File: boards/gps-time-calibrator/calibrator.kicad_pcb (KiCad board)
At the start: 4 copper layers, 180 x 100 mm, 368 parts, among them J1 DF40C-40DP-0.4V(51), J2 DF40C(2.0)-40DS-0.4V(51), J3 USB-C 5V/3A + DATA, J5 GPS ANTENNA, J6 INPUT 5V / 2.5V THRESHOLD, J7 FPGA OUTPUT 5V, J8 61300411121, Q1 AO3400A, Q10 AO3400A, Q11 AO3400A, Q12 AO3400A, Q13 AO3400A, Q14 AO3400A, Q15 AO3400A, Q16 AO3400A, Q2 AO3400A, Q3 AO3400A, Q4 AO3400A, Q5 AO3400A, Q6 AO3400A, Q7 AO3400A, Q8 AO3400A, Q9 AO3400A, U1 USBLC6-2SC6, U10 SN74AHCT1G125DBVR, U11 HUSB238_002DD, U14 TPS259531DSGR, U15 TPS7A4533DCQR, U2 AP2112K-3.3, U3 SN74LVC541APWR, U4 SN74LVC541APWR, U5 AP2112K-3.3, U6 MAX-M10S-00B-01, U7 SN74LVC1G17DBVR, U9 TLV3501AIDBVR, Y1 AOC97FAJC-10.0000

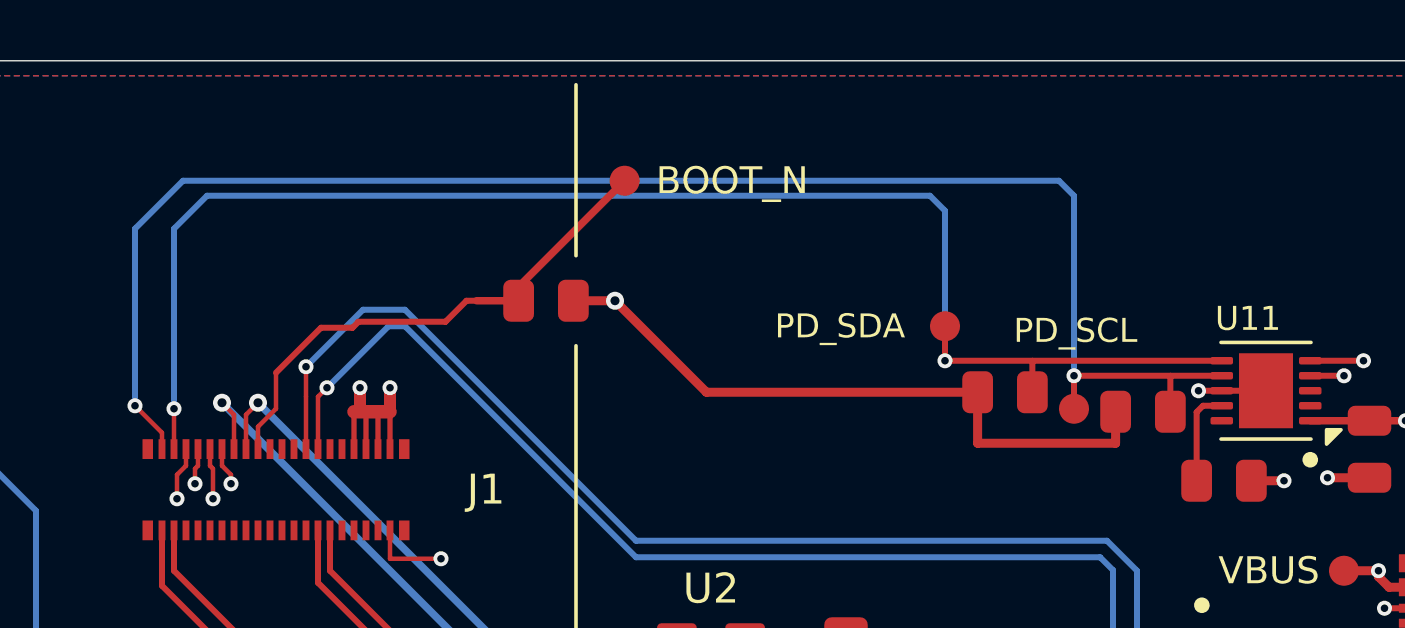
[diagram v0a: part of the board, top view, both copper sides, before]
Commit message: Run the PD I2C pair in parallel with stacked test points and pull-ups
SDA jogs up to a 2 mm pitch beside SCL right off U11, then both lines run
west together through TP10/TP11 (inline, stacked at x 183), a staggered pair
of B.Cu vias, and end on R167/R168 stacked at x 178.6. The pull-up rail
joins both west pads and runs straight to the existing +3V3_LOGIC via.

Co-Authored-By: Claude Opus 5.5 <noreply@anthropic.com>
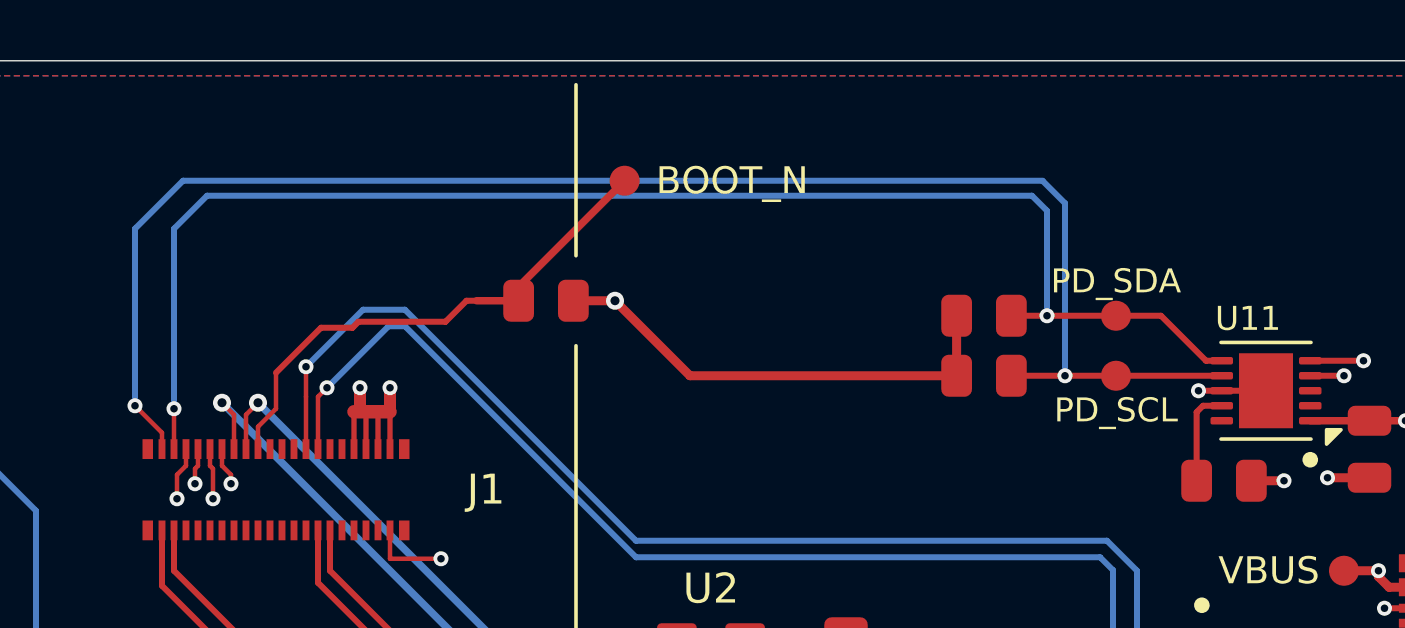
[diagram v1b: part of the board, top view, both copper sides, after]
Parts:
- moved TP10 5.71 mm to (183.0, 18.5)
- moved R168 5.43 mm to (178.6, 20.5)
- moved R167 2.64 mm to (178.6, 18.5)
- moved TP11 1.78 mm to (183.0, 20.5)
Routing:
- net +3V3_LOGIC: track 233.9 -> 227.6 mm
- net USB_PD_SDA: track 50.1 -> 48.2 mm
- net USB_PD_SCL: track 53.1 -> 52.5 mm
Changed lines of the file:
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@@
 	(footprint "Calibrator:TP_1p0mm"
 		(layer "F.Cu")
-		(at 177.3 18.85)
+		(at 183 18.5)
 		(descr "Test pad: PD controller I2C SDA.")
 		(property "Reference" "TP10"
@@
 		)
 		(property "Value" "PD_SDA"
-			(at -3.5 0 0)
+			(at 0 -1.15 0)
 			(layer "F.SilkS")
 			(effects
@@
 	(footprint "Calibrator:R_0805_2012Metric"
 		(layer "F.Cu")
-		(at 183.9 21.7)
+		(at 178.6 20.5)
 		(descr "10 kOhm I2C pull-up on the PD controller's SCL, to +3V3_LOGIC.")
 		(tags "resistor")
@@
 	(footprint "Calibrator:R_0805_2012Metric"
 		(layer "F.Cu")
-		(at 179.3 21.05)
+		(at 178.6 18.5)
 		(descr "10 kOhm I2C pull-up on the PD controller's SDA, to +3V3_LOGIC.")
 		(tags "resistor")
@@
 	(footprint "Calibrator:TP_1p0mm"
 		(layer "F.Cu")
-		(at 181.6 21.6)
+		(at 183 20.5)
 		(descr "Test pad: PD controller I2C SCL.")
 		(property "Reference" "TP11"
@@
 		)
 		(property "Value" "PD_SCL"
-			(at 0.05 -2.6 0)
+			(at 0 1.15 0)
 			(layer "F.SilkS")
 			(effects
@@
 	)
 	(segment
-		(start 178.3875 21.05)
-		(end 169.35 21.05)
-		(width 0.3)
-		(layer "F.Cu")
-		(net "+3V3_LOGIC")
-	)
-	(segment
 		(start 106.55 26.8625)
 		(end 106.55 25.3625)
@@
 	)
 	(segment
-		(start 178.3875 22.75)
-		(end 182.9875 22.75)
-		(width 0.3)
-		(layer "F.Cu")
-		(net "+3V3_LOGIC")
-	)
-	(segment
 		(start 134.05 71)
 		(end 134.05 73.5)
@@
 	)
 	(segment
-		(start 182.9875 22.75)
-		(end 182.9875 21.7)
+		(start 177.6875 18.5)
+		(end 177.6875 20.5)
 		(width 0.3)
 		(layer "F.Cu")
@@
 	)
 	(segment
-		(start 169.35 21.05)
-		(end 166.3 18)
-		(width 0.3)
-		(layer "F.Cu")
-		(net "+3V3_LOGIC")
-	)
-	(segment
 		(start 58.55 26.8625)
 		(end 58.55 25.3625)
@@
 	)
 	(segment
-		(start 178.3875 21.05)
-		(end 178.3875 22.75)
-		(width 0.3)
-		(layer "F.Cu")
-		(net "+3V3_LOGIC")
-	)
-	(segment
 		(start 145.73 71.9125)
 		(end 145.73 75.42)
@@
 	)
 	(segment
+		(start 168.8 20.5)
+		(end 166.3 18)
+		(width 0.3)
+		(layer "F.Cu")
+		(net "+3V3_LOGIC")
+	)
+	(segment
 		(start 134.05 73.5)
 		(end 151 73.5)
@@
 		(net "+3V3_LOGIC")
 	)
+	(segment
+		(start 177.6875 20.5)
+		(end 168.8 20.5)
+		(width 0.3)
+		(layer "F.Cu")
+		(net "+3V3_LOGIC")
+	)
 	(via
 		(at 132 73.5)
@@
 	)
 	(segment
-		(start 180.2125 20)
-		(end 180.2125 21.05)
+		(start 186 20)
+		(end 184.5 18.5)
 		(width 0.2)
 		(layer "F.Cu")
@@
 	)
 	(segment
-		(start 151.6 22.945)
-		(end 151.6 21.6)
-		(width 0.15)
+		(start 184.5 18.5)
+		(end 179.5125 18.5)
+		(width 0.2)
 		(layer "F.Cu")
 		(net "USB_PD_SDA")
@@
 	(segment
 		(start 186.525 20)
-		(end 177.3 20)
+		(end 186 20)
 		(width 0.2)
 		(layer "F.Cu")
@@
 	)
 	(segment
-		(start 177.3 20)
-		(end 177.3 18.85)
-		(width 0.2)
+		(start 151.6 22.945)
+		(end 151.6 21.6)
+		(width 0.15)
 		(layer "F.Cu")
 		(net "USB_PD_SDA")
@@
 	)
 	(via
-		(at 177.3 20)
+		(at 180.7 18.5)
 		(size 0.5)
 		(drill 0.25)
@@
 	)
 	(segment
-		(start 177.3 15)
-		(end 176.8 14.5)
+		(start 180.7 15)
+		(end 180.2 14.5)
 		(width 0.2)
 		(layer "B.Cu")
@@
 	)
 	(segment
-		(start 176.8 14.5)
+		(start 180.2 14.5)
 		(end 152.7 14.5)
 		(width 0.2)
@@
 	)
 	(segment
-		(start 177.3 20)
-		(end 177.3 15)
+		(start 180.7 18.5)
+		(end 180.7 15)
 		(width 0.2)
 		(layer "B.Cu")
@@
 	)
 	(segment
-		(start 184.8125 20.5)
-		(end 184.8125 21.7)
-		(width 0.2)
-		(layer "F.Cu")
-		(net "USB_PD_SCL")
-	)
-	(segment
 		(start 186.525 20.5)
-		(end 181.6 20.5)
+		(end 179.5125 20.5)
 		(width 0.2)
 		(layer "F.Cu")
@@
 		(net "USB_PD_SCL")
 	)
-	(segment
-		(start 181.6 20.5)
-		(end 181.6 21.6)
-		(width 0.2)
-		(layer "F.Cu")
-		(net "USB_PD_SCL")
-	)
 	(via
-		(at 181.6 20.5)
+		(at 181.3 20.5)
 		(size 0.5)
 		(drill 0.25)
@@
 	)
 	(segment
-		(start 181.1 14)
+		(start 180.55 14)
 		(end 151.9 14)
 		(width 0.2)
@@
 	)
 	(segment
-		(start 181.6 14.5)
-		(end 181.1 14)
+		(start 150.3 15.6)
+		(end 151.9 14)
 		(width 0.2)
 		(layer "B.Cu")
@@
 	)
 	(segment
-		(start 181.6 20.5)
-		(end 181.6 14.5)
+		(start 150.3 21.5)
+		(end 150.3 15.6)
 		(width 0.2)
 		(layer "B.Cu")
@@
 	)
 	(segment
-		(start 150.3 15.6)
-		(end 151.9 14)
+		(start 181.3 14.75)
+		(end 180.55 14)
 		(width 0.2)
 		(layer "B.Cu")
@@
 	)
 	(segment
-		(start 150.3 21.5)
-		(end 150.3 15.6)
+		(start 181.3 20.5)
+		(end 181.3 14.75)
 		(width 0.2)
 		(layer "B.Cu")

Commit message: Move +3V3_LOGIC off In2 onto the outer layers
The rail now runs on F.Cu: U2 up to R4 and the PD pull-ups, a strip along
the top edge to the FPGA bus, one short B.Cu hop across the bus, then F.Cu
along y 23 past U3/U4/R140 and down x 132 to the OLED header. Six inner-layer
vias drop to the two at the bus crossing; no In1/In2 copper left on the net.

Co-Authored-By: Claude Opus 5.5 <noreply@anthropic.com>
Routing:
- net +3V3_LOGIC: track 227.6 -> 258.5 mm, vias 6 -> 2
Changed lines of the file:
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@@
 		(start 151 71.9125)
 		(end 151 73.5)
-		(width 0.35)
-		(layer "F.Cu")
-		(net "+3V3_LOGIC")
-	)
-	(segment
-		(start 106.55 26.8625)
-		(end 106.55 25.3625)
-		(width 0.35)
+		(width 0.4)
+		(layer "F.Cu")
+		(net "+3V3_LOGIC")
+	)
+	(segment
+		(start 106.55 26.863)
+		(end 106.55 23)
+		(width 0.4)
+		(layer "F.Cu")
+		(net "+3V3_LOGIC")
+	)
+	(segment
+		(start 58.55 23.5)
+		(end 58.55 26.863)
+		(width 0.4)
+		(layer "F.Cu")
+		(net "+3V3_LOGIC")
+	)
+	(segment
+		(start 136.4 13.5)
+		(end 136.4 24)
+		(width 0.4)
 		(layer "F.Cu")
 		(net "+3V3_LOGIC")
@@
 	)
 	(segment
-		(start 177.6875 18.5)
-		(end 177.6875 20.5)
-		(width 0.3)
+		(start 177.6875 20.5)
+		(end 166.3 20.5)
+		(width 0.4)
+		(layer "F.Cu")
+		(net "+3V3_LOGIC")
+	)
+	(segment
+		(start 59.05 23)
+		(end 114.088 23)
+		(width 0.4)
+		(layer "F.Cu")
+		(net "+3V3_LOGIC")
+	)
+	(segment
+		(start 114.088 23.8)
+		(end 115.651 25.363)
+		(width 0.4)
+		(layer "F.Cu")
+		(net "+3V3_LOGIC")
+	)
+	(segment
+		(start 177.688 20.5)
+		(end 177.688 13.5)
+		(width 0.4)
+		(layer "F.Cu")
+		(net "+3V3_LOGIC")
+	)
+	(segment
+		(start 176.6875 12.5)
+		(end 137.4 12.5)
+		(width 0.4)
+		(layer "F.Cu")
+		(net "+3V3_LOGIC")
+	)
+	(segment
+		(start 137.4 12.5)
+		(end 136.4 13.5)
+		(width 0.4)
 		(layer "F.Cu")
 		(net "+3V3_LOGIC")
@@
 	)
 	(segment
-		(start 145.73 71.9125)
-		(end 145.73 73.5)
-		(width 0.35)
-		(layer "F.Cu")
-		(net "+3V3_LOGIC")
-	)
-	(segment
 		(start 168.3625 30.95)
 		(end 168.363 32.6)
-		(width 0.3)
-		(layer "F.Cu")
-		(net "+3V3_LOGIC")
-	)
-	(segment
-		(start 58.55 26.8625)
-		(end 58.55 25.3625)
-		(width 0.35)
+		(width 0.4)
+		(layer "F.Cu")
+		(net "+3V3_LOGIC")
+	)
+	(segment
+		(start 132 31.6)
+		(end 132 72.5)
+		(width 0.4)
+		(layer "F.Cu")
+		(net "+3V3_LOGIC")
+	)
+	(segment
+		(start 166.3 30.05)
+		(end 166.3 18)
+		(width 0.4)
+		(layer "F.Cu")
+		(net "+3V3_LOGIC")
+	)
+	(segment
+		(start 167.2 30.95)
+		(end 166.3 30.05)
+		(width 0.4)
 		(layer "F.Cu")
 		(net "+3V3_LOGIC")
@@
 		(start 168.3625 30.95)
 		(end 167.2 30.95)
-		(width 0.3)
-		(layer "F.Cu")
-		(net "+3V3_LOGIC")
-	)
-	(segment
-		(start 132 73.5)
-		(end 134.05 73.5)
-		(width 0.5)
+		(width 0.4)
+		(layer "F.Cu")
+		(net "+3V3_LOGIC")
+	)
+	(segment
+		(start 132 72.5)
+		(end 133 73.5)
+		(width 0.4)
+		(layer "F.Cu")
+		(net "+3V3_LOGIC")
+	)
+	(segment
+		(start 125.763 25.363)
+		(end 132 31.6)
+		(width 0.4)
 		(layer "F.Cu")
 		(net "+3V3_LOGIC")
@@
 		(start 104.575 26.8625)
 		(end 106.55 26.8625)
-		(width 0.35)
+		(width 0.4)
 		(layer "F.Cu")
 		(net "+3V3_LOGIC")
@@
 		(start 56.575 26.8625)
 		(end 58.55 26.8625)
-		(width 0.35)
+		(width 0.4)
+		(layer "F.Cu")
+		(net "+3V3_LOGIC")
+	)
+	(segment
+		(start 115.651 25.363)
+		(end 125.763 25.363)
+		(width 0.4)
+		(layer "F.Cu")
+		(net "+3V3_LOGIC")
+	)
+	(segment
+		(start 114.088 23)
+		(end 114.088 23.8)
+		(width 0.4)
 		(layer "F.Cu")
 		(net "+3V3_LOGIC")
@@
 		(start 145.73 71.9125)
 		(end 145.73 75.42)
-		(width 0.35)
+		(width 0.4)
 		(layer "F.Cu")
 		(net "+3V3_LOGIC")
@@
 		(start 168.363 32.6)
 		(end 170.6 32.6)
-		(width 0.3)
-		(layer "F.Cu")
-		(net "+3V3_LOGIC")
-	)
-	(segment
-		(start 168.8 20.5)
-		(end 166.3 18)
-		(width 0.3)
+		(width 0.4)
+		(layer "F.Cu")
+		(net "+3V3_LOGIC")
+	)
+	(segment
+		(start 58.55 23.5)
+		(end 59.05 23)
+		(width 0.4)
 		(layer "F.Cu")
 		(net "+3V3_LOGIC")
@@
 		(start 134.05 73.5)
 		(end 151 73.5)
-		(width 0.5)
-		(layer "F.Cu")
-		(net "+3V3_LOGIC")
-	)
-	(segment
-		(start 114.0875 23)
-		(end 114.0875 25.3625)
-		(width 0.35)
+		(width 0.4)
+		(layer "F.Cu")
+		(net "+3V3_LOGIC")
+	)
+	(segment
+		(start 177.6875 13.5)
+		(end 176.6875 12.5)
+		(width 0.4)
+		(layer "F.Cu")
+		(net "+3V3_LOGIC")
+	)
+	(segment
+		(start 133 73.5)
+		(end 134.05 73.5)
+		(width 0.4)
 		(layer "F.Cu")
 		(net "+3V3_LOGIC")
@@
 		(start 164.9125 18)
 		(end 166.3 18)
-		(width 0.3)
-		(layer "F.Cu")
-		(net "+3V3_LOGIC")
-	)
-	(segment
-		(start 177.6875 20.5)
-		(end 168.8 20.5)
-		(width 0.3)
+		(width 0.4)
 		(layer "F.Cu")
 		(net "+3V3_LOGIC")
 	)
 	(via
-		(at 132 73.5)
-		(size 0.6)
-		(drill 0.3)
-		(layers "F.Cu" "B.Cu")
-		(net "+3V3_LOGIC")
-	)
-	(via
-		(at 106.55 25.3625)
+		(at 130.4 30)
 		(size 0.5)
 		(drill 0.25)
@@
 	)
 	(via
-		(at 114.0875 25.3625)
+		(at 136.4 24)
 		(size 0.5)
 		(drill 0.25)
@@
 		(net "+3V3_LOGIC")
 	)
-	(via
-		(at 167.2 30.95)
-		(size 0.5)
-		(drill 0.25)
-		(layers "F.Cu" "B.Cu")
-		(net "+3V3_LOGIC")
-	)
-	(via
-		(at 166.3 18)
-		(size 0.6)
-		(drill 0.3)
-		(layers "F.Cu" "B.Cu")
-		(net "+3V3_LOGIC")
-	)
-	(via
-		(at 58.55 25.3625)
-		(size 0.5)
-		(drill 0.25)
-		(layers "F.Cu" "B.Cu")
-		(net "+3V3_LOGIC")
-	)
-	(segment
-		(start 166.3 18)
-		(end 166.3 30.05)
-		(width 0.5)
-		(layer "In2.Cu")
-		(net "+3V3_LOGIC")
-	)
-	(segment
-		(start 166.55 31.6)
-		(end 158 31.6)
-		(width 0.6)
-		(layer "In2.Cu")
-		(net "+3V3_LOGIC")
-	)
-	(segment
-		(start 158 31.6)
-		(end 132 31.6)
-		(width 0.6)
-		(layer "In2.Cu")
-		(net "+3V3_LOGIC")
-	)
-	(segment
-		(start 132 31.6)
-		(end 132 73.5)
-		(width 0.6)
-		(layer "In2.Cu")
-		(net "+3V3_LOGIC")
-	)
-	(segment
-		(start 106.55 25.3625)
-		(end 125.7625 25.3625)
-		(width 0.5)
-		(layer "In2.Cu")
-		(net "+3V3_LOGIC")
-	)
-	(segment
-		(start 167.2 30.95)
-		(end 166.55 31.6)
-		(width 0.6)
-		(layer "In2.Cu")
-		(net "+3V3_LOGIC")
-	)
-	(segment
-		(start 58.55 25.3625)
-		(end 106.55 25.3625)
-		(width 0.5)
-		(layer "In2.Cu")
-		(net "+3V3_LOGIC")
-	)
-	(segment
-		(start 166.3 30.05)
-		(end 167.2 30.95)
-		(width 0.5)
-		(layer "In2.Cu")
-		(net "+3V3_LOGIC")
-	)
-	(segment
-		(start 125.7625 25.3625)
-		(end 132 31.6)
-		(width 0.5)
-		(layer "In2.Cu")
-		(net "+3V3_LOGIC")
-	)
+	(segment
+		(start 136.4 24)
+		(end 130.4 30)
+		(width 0.4)
+		(layer "B.Cu")
+		(net "+3V3_LOGIC")
+	)

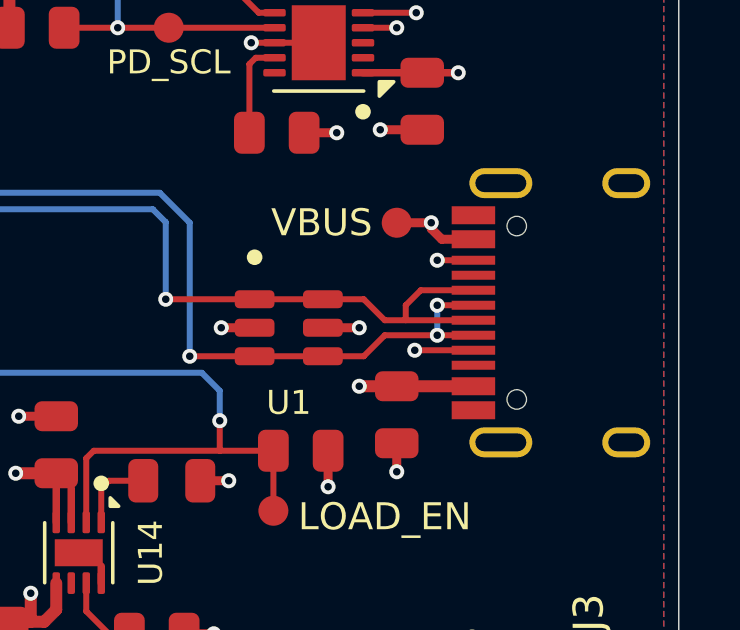
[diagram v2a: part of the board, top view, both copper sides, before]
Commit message: Cross USB D- under the USB-C receptacle
The B7-to-A7 D- jumper now drops to B.Cu just past the pad tips under J3's
body instead of in front of the connector, and the D+ B6-to-A6 link tucks
in to x 191.7 now that the A7 stub no longer runs west.

Co-Authored-By: Claude Opus 5.5 <noreply@anthropic.com>
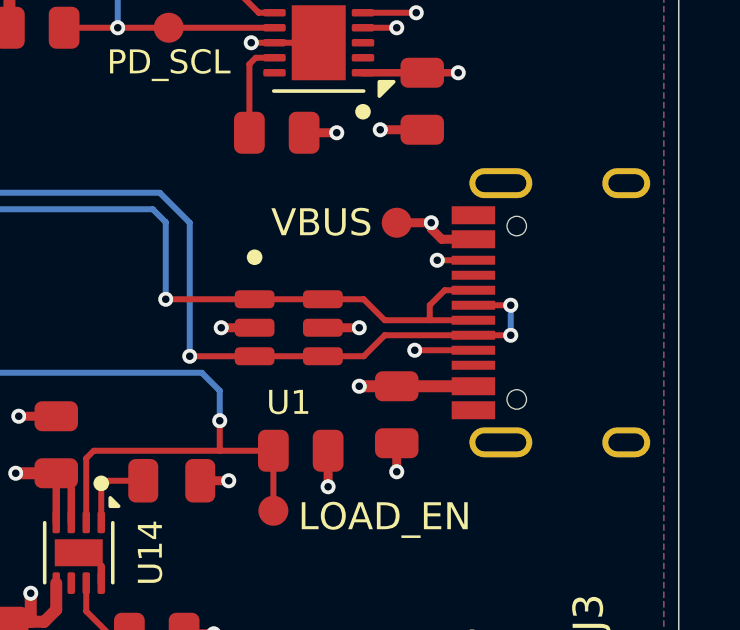
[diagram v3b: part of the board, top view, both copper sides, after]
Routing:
- net USB_D-: track 51.2 -> 52.5 mm
- net USB_D+: track 48.7 -> 47.9 mm
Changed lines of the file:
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@@
+	)
+	(segment
+		(start 193.155 29.25)
+		(end 192.2 29.25)
+		(width 0.2)
+		(layer "F.Cu")
+		(net "USB_D+")
+	)
+	(segment
+		(start 191.7 29.75)
+		(end 191.7 30.25)
+		(width 0.2)
+		(layer "F.Cu")
+		(net "USB_D+")
 	)
 	(segment
@@
 	)
 	(segment
-		(start 193.155 29.25)
-		(end 191.4 29.25)
-		(width 0.2)
-		(layer "F.Cu")
-		(net "USB_D+")
-	)
-	(segment
 		(start 190.2 30.25)
 		(end 189.5 29.55)
@@
 	)
 	(segment
-		(start 191.4 29.25)
-		(end 190.9 29.75)
-		(width 0.2)
-		(layer "F.Cu")
-		(net "USB_D+")
-	)
-	(segment
-		(start 190.9 29.75)
-		(end 190.9 30.25)
+		(start 192.2 29.25)
+		(end 191.7 29.75)
 		(width 0.2)
 		(layer "F.Cu")
@@
 	(segment
 		(start 193.155 29.75)
-		(end 191.95 29.75)
-		(width 0.2)
-		(layer "F.Cu")
-		(net "USB_D-")
-	)
-	(segment
-		(start 193.155 30.75)
+		(end 194.4 29.75)
+		(width 0.2)
+		(layer "F.Cu")
+		(net "USB_D-")
+	)
+	(segment
+		(start 194.4 30.75)
 		(end 190.2 30.75)
 		(width 0.2)
@@
 	)
 	(via
-		(at 191.95 29.75)
-		(size 0.5)
-		(drill 0.25)
-		(layers "F.Cu" "B.Cu")
-		(net "USB_D-")
-	)
-	(via
-		(at 191.95 30.75)
+		(at 194.4 29.75)
 		(size 0.5)
 		(drill 0.25)
@@
 	(via
 		(at 183.7 31.45)
+		(size 0.5)
+		(drill 0.25)
+		(layers "F.Cu" "B.Cu")
+		(net "USB_D-")
+	)
+	(via
+		(at 194.4 30.75)
 		(size 0.5)
 		(drill 0.25)
@@
 	)
 	(segment
-		(start 191.95 29.75)
-		(end 191.95 30.75)
-		(width 0.2)
-		(layer "B.Cu")
+		(start 194.4 29.75)
+		(end 194.4 30.75)
+		(width 0.2)
+		(layer "B.Cu")
